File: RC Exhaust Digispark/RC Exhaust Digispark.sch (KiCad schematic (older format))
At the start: 12 parts, among them J5 THR, J6 THR_Y

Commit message: Digispark dashboard sketch
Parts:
- R1: value 270 -> 220
- R2: value 270 -> 200
- R3: value 270 -> 150
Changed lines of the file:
@@
 P 7900 2725
 F 0 "R1" H 7959 2771 50  0000 L CNN
-F 1 "270" H 7959 2680 50  0000 L CNN
+F 1 "220" H 7959 2680 50  0000 L CNN
 F 2 "resistor:R_Axial_DIN0207_L6.3mm_D2.5mm_P7.62mm_Horizontal" H 7900 2725 50  0001 C CNN
 F 3 "~" H 7900 2725 50  0001 C CNN
@@
 P 8350 2725
 F 0 "R2" H 8409 2771 50  0000 L CNN
-F 1 "270" H 8409 2680 50  0000 L CNN
+F 1 "200" H 8409 2680 50  0000 L CNN
 F 2 "resistor:R_Axial_DIN0207_L6.3mm_D2.5mm_P7.62mm_Horizontal" H 8350 2725 50  0001 C CNN
 F 3 "~" H 8350 2725 50  0001 C CNN
@@
 P 8800 2725
 F 0 "R3" H 8859 2771 50  0000 L CNN
-F 1 "270" H 8859 2680 50  0000 L CNN
+F 1 "150" H 8859 2680 50  0000 L CNN
 F 2 "resistor:R_Axial_DIN0207_L6.3mm_D2.5mm_P7.62mm_Horizontal" H 8800 2725 50  0001 C CNN
 F 3 "~" H 8800 2725 50  0001 C CNN

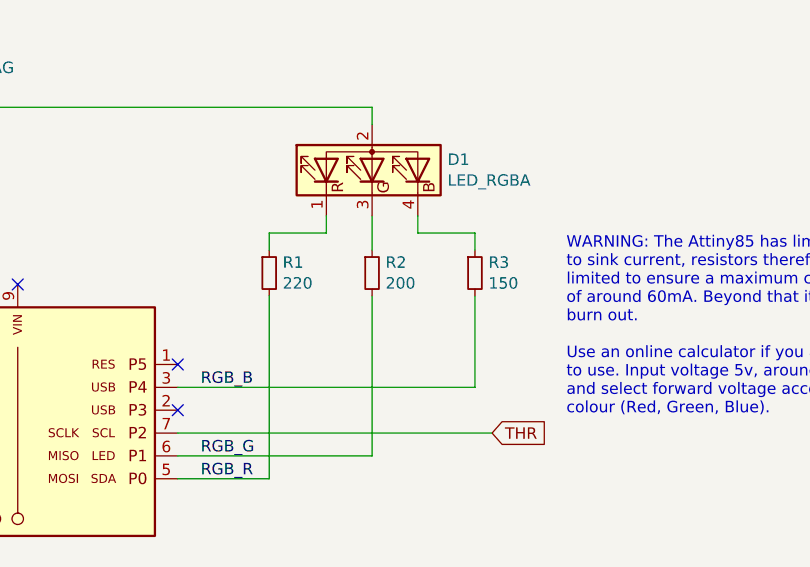
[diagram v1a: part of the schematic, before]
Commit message: Small exhaust tweaks to better fit Digistump into computers
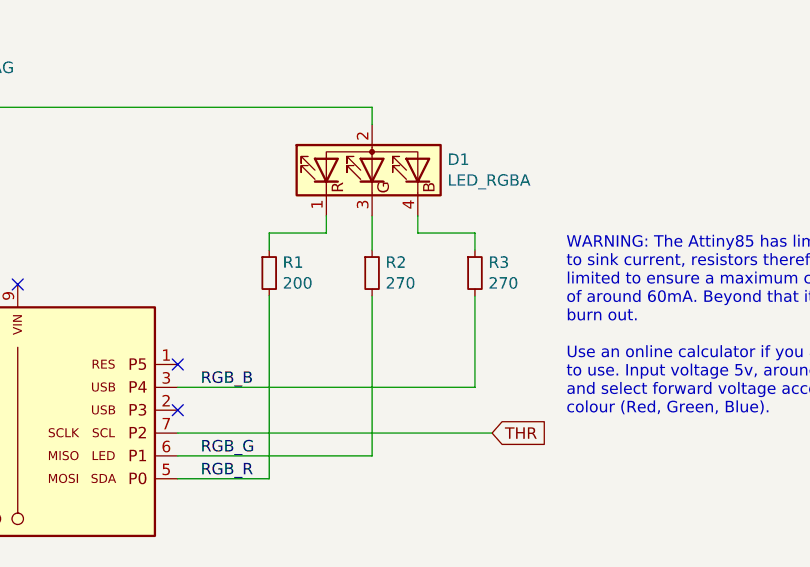
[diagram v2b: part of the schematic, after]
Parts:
- R1: value 220 -> 200
- R2: value 200 -> 270
- R3: value 150 -> 270
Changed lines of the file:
@@
 P 7900 2725
 F 0 "R1" H 7959 2771 50  0000 L CNN
-F 1 "220" H 7959 2680 50  0000 L CNN
+F 1 "200" H 7959 2680 50  0000 L CNN
 F 2 "resistor:R_Axial_DIN0207_L6.3mm_D2.5mm_P7.62mm_Horizontal" H 7900 2725 50  0001 C CNN
 F 3 "~" H 7900 2725 50  0001 C CNN
 	1    7900 2725
-	1    0    0    -1
-$EndComp
-$Comp
-L Device:R_Small R2
-U 1 1 64ED38BC
-P 8350 2725
-F 0 "R2" H 8409 2771 50  0000 L CNN
-F 1 "200" H 8409 2680 50  0000 L CNN
-F 2 "resistor:R_Axial_DIN0207_L6.3mm_D2.5mm_P7.62mm_Horizontal" H 8350 2725 50  0001 C CNN
-F 3 "~" H 8350 2725 50  0001 C CNN
-	1    8350 2725
-	1    0    0    -1
-$EndComp
-$Comp
-L Device:R_Small R3
-U 1 1 650115B7
-P 8800 2725
-F 0 "R3" H 8859 2771 50  0000 L CNN
-F 1 "150" H 8859 2680 50  0000 L CNN
-F 2 "resistor:R_Axial_DIN0207_L6.3mm_D2.5mm_P7.62mm_Horizontal" H 8800 2725 50  0001 C CNN
-F 3 "~" H 8800 2725 50  0001 C CNN
-	1    8800 2725
 	1    0    0    -1
 $EndComp
@@
 Text Notes 9200 3350 0    50   ~ 0
 WARNING: The Attiny85 has limited capability\nto sink current, resistors therefore need to be \nlimited to ensure a maximum combined current\nof around 60mA. Beyond that it will most likely\nburn out.\n\nUse an online calculator if you are unsure what\nto use. Input voltage 5v, around 15mA per LED\nand select forward voltage according to the\ncolour (Red, Green, Blue).
+$Comp
+L Device:R_Small R3
+U 1 1 650115B7
+P 8800 2725
+F 0 "R3" H 8859 2771 50  0000 L CNN
+F 1 "270" H 8859 2680 50  0000 L CNN
+F 2 "resistor:R_Axial_DIN0207_L6.3mm_D2.5mm_P7.62mm_Horizontal" H 8800 2725 50  0001 C CNN
+F 3 "~" H 8800 2725 50  0001 C CNN
+	1    8800 2725
+	1    0    0    -1
+$EndComp
+$Comp
+L Device:R_Small R2
+U 1 1 64ED38BC
+P 8350 2725
+F 0 "R2" H 8409 2771 50  0000 L CNN
+F 1 "270" H 8409 2680 50  0000 L CNN
+F 2 "resistor:R_Axial_DIN0207_L6.3mm_D2.5mm_P7.62mm_Horizontal" H 8350 2725 50  0001 C CNN
+F 3 "~" H 8350 2725 50  0001 C CNN
+	1    8350 2725
+	1    0    0    -1
+$EndComp
 $EndSCHEMATC
